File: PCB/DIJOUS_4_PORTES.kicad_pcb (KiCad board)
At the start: 2 copper layers, 180.4 x 120 mm, 59 parts, among them J1 PowerIN, J10 DOOR_LCK, J12 WIN_SW, J13 JTAG, J14 FINAL_CARRERA_UP, J15 FINAL_CARRERA_DOWN, J2 OUT_WIN, J3 ICSP, J4 CAN, J5 OUT_DOOR, J6 USART, J7 SPI, J8 RFID_COAX, SW1 DOOR_LCK, SW3 WIN_SW, U2 PIC32MK0256MCJ048-I/Y8X, U3 TCAN334D, U4 MAX22201ATC+, U5 MAX22201ATC+, Y1 ECS-3225SMV-080-GP-TR, Y2 ECS-3225SMV-080-GP-TR

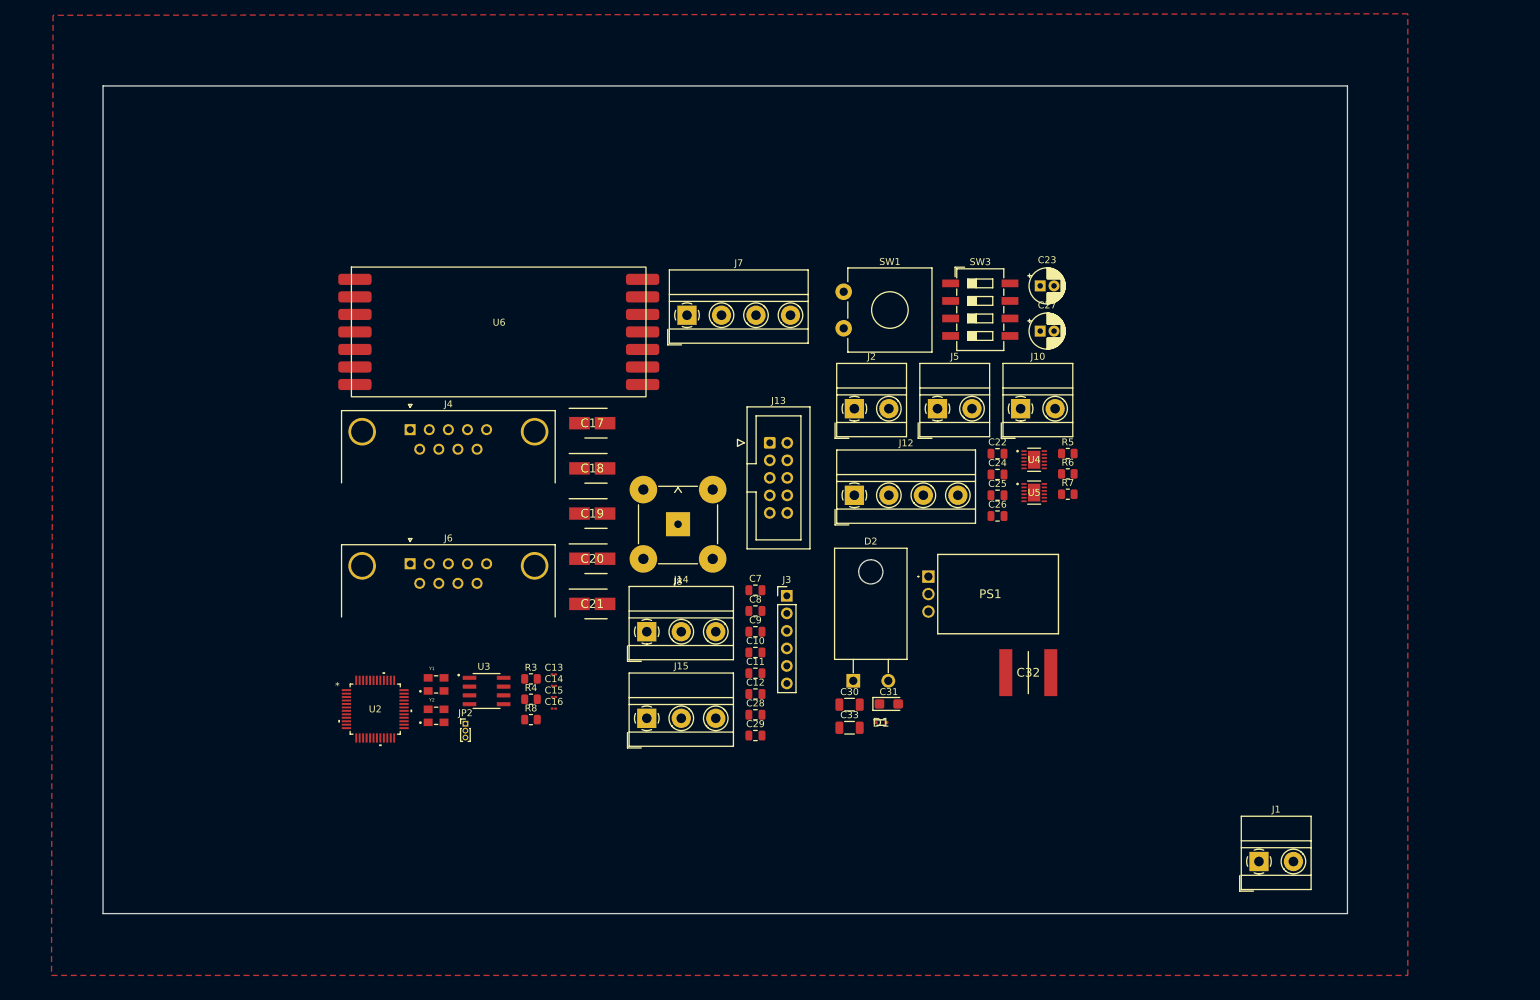
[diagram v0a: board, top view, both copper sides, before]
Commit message: power plane done
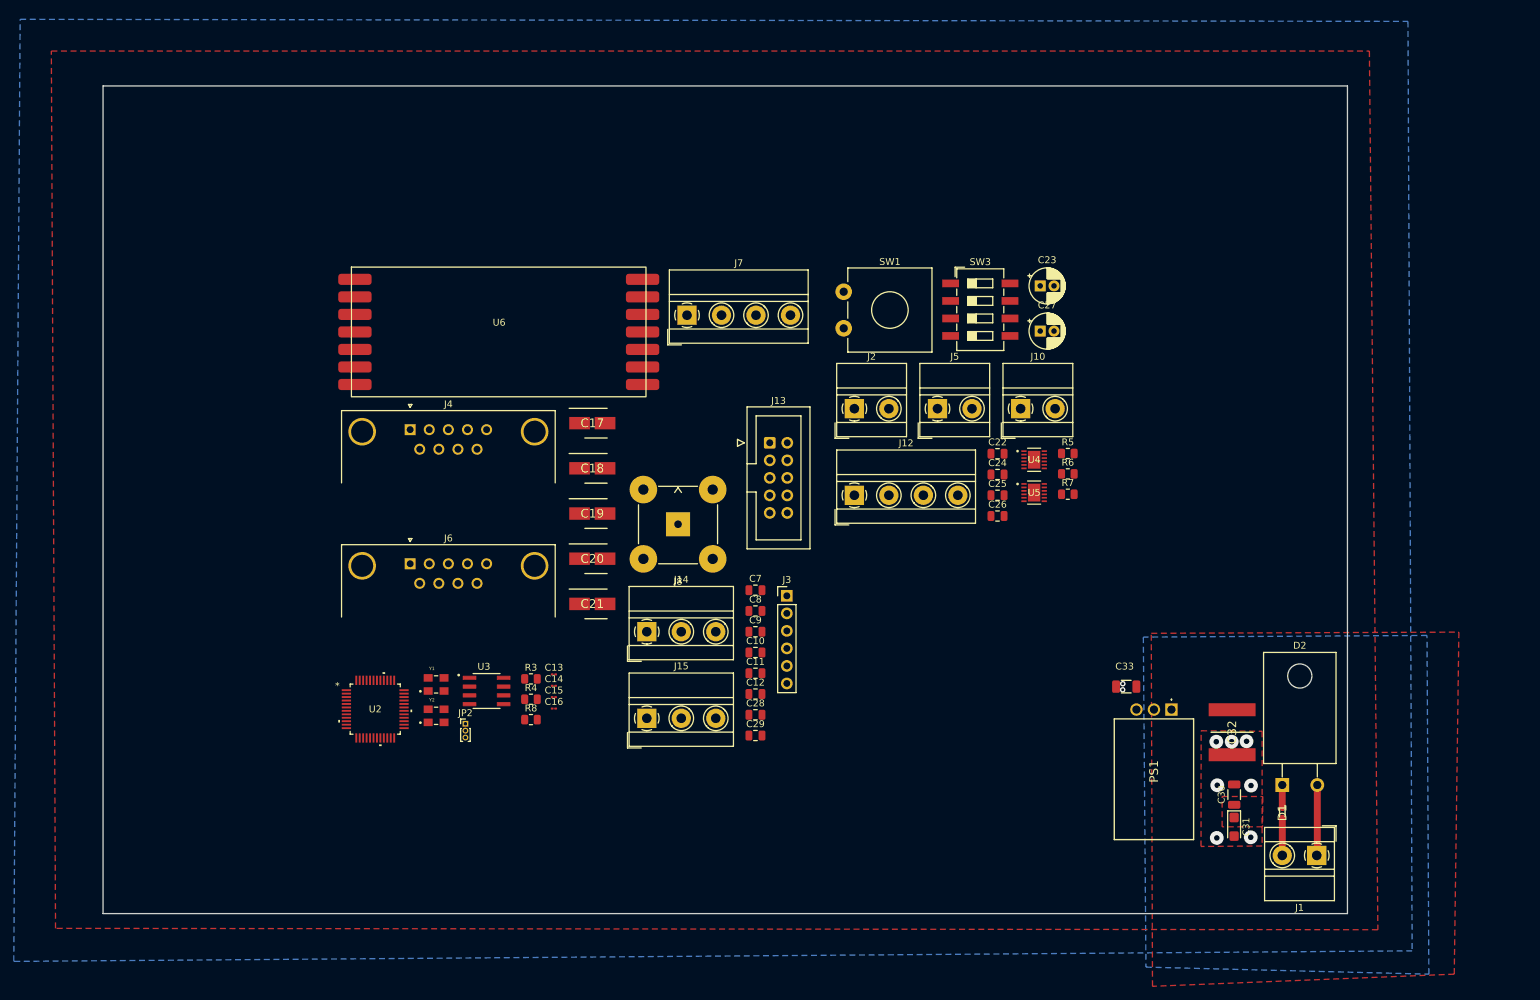
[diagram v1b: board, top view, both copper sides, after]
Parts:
- moved D2 64.0 mm to (231.1, 141.3)
- moved D1 59.6 mm to (231.1, 145.4), turned to -90 degrees
- moved C30 57.3 mm to (224.1, 142.7), turned to 90 degrees
- moved C31 53.1 mm to (224.1, 147.4), turned to -90 degrees
- moved C33 40.5 mm to (208.5, 127.1), turned to 180 degrees
- moved PS1 40.2 mm to (215.0, 130.4), turned to -90 degrees
- moved C32 30.8 mm to (223.8, 133.7), turned to -90 degrees
- moved J1 8.43 mm to (236.1, 151.6), turned to 180 degrees
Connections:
- net Net-(C12-Pad1) renamed /DIGITAL/MCLR_VDD
- net Net-(D2-A) renamed /PWR IN/pwin
- net Net-(J3-VDD) renamed /DIGITAL/Vdd_icsp
- net Net-(J8-In) renamed /DIGITAL/RF_out
- net Net-(U2-OSCI/CLKI/AN49/CVD49/RPC12/RC12') renamed /DIGITAL/clk1i
- net Net-(U2-OSCO/CLKO/RPC15/RC15) renamed /DIGITAL/clk1o
- net Net-(U2-SOSCI/RPC13/RC13) renamed /DIGITAL/clk2i
- net Net-(U2-SOSCO/RPB8/T1CK/RB8) renamed /DIGITAL/clk2o
- C18 pad 1: VDD -> VDDA
- C9 pad 2: VDD -> VDDA
- U2 pad 10: WIN_IN3 -> WIN_SW3
- U2 pad 15: VDD -> VDDA
- U2 pad 9: ISEN -> ISEN_WIN
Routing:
- net /PWR IN/pwin: track 0.00 -> 10.2 mm
- net GNDPWR: track 0.00 -> 5.84 mm, vias 0 -> 7
- net +12V: track 0.00 -> 3.26 mm
- net GND: track 0.00 -> 2.31 mm, vias 0 -> 2
- added copper zone on F.Cu, net +12V
- added copper zone on F.Cu, net +3.3V
- added copper zone on B.Cu, net GND
- added copper zone on B.Cu, net GNDPWR
- added copper zone on F.Cu, net GNDPWR
- removed copper zone on F.Cu, net GND

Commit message: start digital
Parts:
- moved J13 91.6 mm to (66.6, 75.8)
- moved J14 85.2 mm to (90.4, 49.2)
- moved J15 85.2 mm to (90.4, 61.7)
- moved J7 82.5 mm to (66.2, 48.2)
- moved J3 79.7 mm to (234.7, 88.3)
- moved Y1 56.4 mm to (164.4, 119.1), turned to 90 degrees
- moved Y2 56.1 mm to (164.5, 132.6), turned to -90 degrees
- moved U2 53.0 mm to (152.5, 126.1)
- moved J6 46.4 mm to (68.3, 138.1), turned to -90 degrees
- moved C16 42.5 mm to (166.8, 119.8)
- moved C14 40.8 mm to (165.4, 135.4), turned to -90 degrees
- moved C15 39.8 mm to (163.4, 116.5), turned to 90 degrees
- moved J4 39.5 mm to (68.3, 105.2), turned to -90 degrees
- moved C13 37.2 mm to (162.1, 132.0), turned to 180 degrees
- moved J2 36.4 mm to (197.5, 64.1)
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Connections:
- C18 pad 2: GND -> GNDA
- C9 pad 1: GND -> GNDA
- U2 pad 16: GND -> GNDA
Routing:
- net VDD: track 0.00 -> 17.4 mm
- net GND: track 2.31 -> 19.4 mm, vias 2 -> 46
- net /DIGITAL/clk1o: track 0.00 -> 14.7 mm
- net /DIGITAL/clk2o: track 0.00 -> 13.8 mm
- net +3.3V: track 0.00 -> 13.4 mm
- net /DIGITAL/clk2i: track 0.00 -> 11.9 mm
- net /DIGITAL/clk1i: track 0.00 -> 11.5 mm
- net SPI_CK: track 0.00 -> 3.83 mm, vias 0 -> 1
- net GNDA: track 0.00 -> 3.16 mm, vias 0 -> 2
- net SPI_SDI: track 0.00 -> 2.96 mm, vias 0 -> 1
- net GNDPWR: track 5.84 -> 8.43 mm
- net SPI_SDO: track 0.00 -> 2.08 mm, vias 0 -> 1
- net WIN_SW1: track 0.00 -> 1.37 mm, vias 0 -> 1
- net SPI_SS: track 0.00 -> 1.36 mm, vias 0 -> 1
- added copper zone on F.Cu, net GND
- added copper zone on B.Cu, net GNDA
- added copper zone on F.Cu, net VDD

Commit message: changed clks, pwr
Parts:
- removed C13, C14, C15, C16: 21p, Capacitor_SMD:C_01005_0402Metric
- removed J13: JTAG, Connector_IDC:IDC-Header_2x05_P2.54mm_Vertical
- added C1: 1u, Capacitor_SMD:C_0805_2012Metric, F.Cu at (202.1, 140.9)
- added C2: 100n, Capacitor_SMD:C_0805_2012Metric, F.Cu at (204.5, 140.9)
- added C3: 47u, Capacitor_THT:CP_Radial_D5.0mm_P2.00mm, F.Cu at (198.1, 154.8)
- added C4: 47u, Capacitor_THT:CP_Radial_D5.0mm_P2.00mm, F.Cu at (198.1, 148.2)
- added C5: 47u, Capacitor_THT:CP_Radial_D5.0mm_P2.00mm, F.Cu at (198.1, 141.7)
- added C6: 47u, Capacitor_THT:CP_Radial_D5.0mm_P2.00mm, F.Cu at (198.1, 135.1)
- added R_LDO1: 330, Resistor_SMD:R_0805_2012Metric_Pad1.20x1.40mm_HandSolder, F.Cu at (204.5, 136.1)
- added U1: LT1528CT-PBF, kicad_models:LT1528CT#PBF, F.Cu at (206.7, 135.1)
- PS1: value P7803-2000R-S -> P7805-2000R-S
- Y1: value ECS-3225SMV-080-GP-TR -> ASZKDV-32.768KHZ-L-T3; footprint kicad_models:OSC_ECS-3225SMV-080-GP-TR -> kicad_models:ASZKDV_ABR
- moved C22 110.4 mm to (113.2, 104.5)
- moved C23 110.4 mm to (119.4, 80.2)
- moved C24 110.4 mm to (113.2, 107.5)
- moved C25 110.4 mm to (113.2, 110.5)
- moved C26 110.4 mm to (113.2, 113.5)
- moved C27 110.4 mm to (119.4, 86.7)
- moved J12 110.4 mm to (92.4, 110.5)
- moved J2 110.4 mm to (92.4, 98.0)
- moved R5 110.4 mm to (123.4, 104.5)
- moved R6 110.4 mm to (123.4, 107.4)
- moved R7 110.4 mm to (123.4, 110.4)
- moved SW3 110.4 mm to (110.7, 83.6)
- moved J10 110.4 mm to (116.5, 98.0)
- moved J3 110.4 mm to (129.6, 122.2)
- moved J5 110.4 mm to (104.5, 98.0)
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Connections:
- C10 pad 1: VDD -> +3.3V
- C11 pad 1: VDD -> +3.3V
- C17 pad 1: VDD -> +3.3V
- C18 pad 1: VDDA -> +3.3V
- C18 pad 2: GNDA -> GND
- C19 pad 1: VDD -> +3.3V
- C20 pad 1: VDD -> +3.3V
- C21 pad 1: VDD -> +3.3V
- C33 pad 1: +3.3V -> +5V
- C33 pad 2: GND -> GNDPWR
- C7 pad 1: VDD -> +3.3V
- C8 pad 1: VDD -> +3.3V
- C9 pad 1: GNDA -> GND
- C9 pad 2: VDDA -> +3.3V
- J3 pad 2: /DIGITAL/Vdd_icsp -> +3.3V
- PS1 pad 3: +3.3V -> +5V
- R3 pad 2: VDD -> +3.3V
- U2 pad 15: VDDA -> +3.3V
- U2 pad 16: GNDA -> GND
- U2 pad 22: VDD -> +3.3V
- U2 pad 26: VDD -> +3.3V
- U2 pad 28: /DIGITAL/clk1o -> unconnected-(U2-OSCO/CLKO/RPC15/RC15-Pad28)
- U2 pad 36: /DIGITAL/clk2o -> FINAL_CARRERA_DOWN
- U2 pad 39: FINAL_CARRERA -> FINAL_CARRERA_UP
- U2 pad 43: VDD -> +3.3V
- U2 pad 6: VDD -> +3.3V
- Y1 pad 3: /DIGITAL/clk2o -> +3.3V
- Y2 pad 1: /DIGITAL/clk1i -> unconnected-(Y2-TRI-STATE-Pad1)
- Y2 pad 3: /DIGITAL/clk1o -> /DIGITAL/clk1i
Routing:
- net +3.3V: track 13.4 -> 71.5 mm
- net +5V: track 0.00 -> 23.3 mm
- net VDD: track 17.4 -> 0.00 mm
- net /DIGITAL/clk1o: track 14.7 -> 0.00 mm
- net /DIGITAL/clk2o: track 13.8 -> 0.00 mm
- net GNDA: track 3.16 -> 0.00 mm, vias 2 -> 0
- net /DIGITAL/clk1i: track 11.5 -> 9.42 mm
- net /DIGITAL/clk2i: track 11.9 -> 10.2 mm
- net GND: track 19.4 -> 20.1 mm, vias 46 -> 61
- net GNDPWR: track 8.43 -> 8.15 mm, vias 7 -> 9
- removed copper zone on B.Cu, net GNDA
- removed copper zone on F.Cu, net VDD

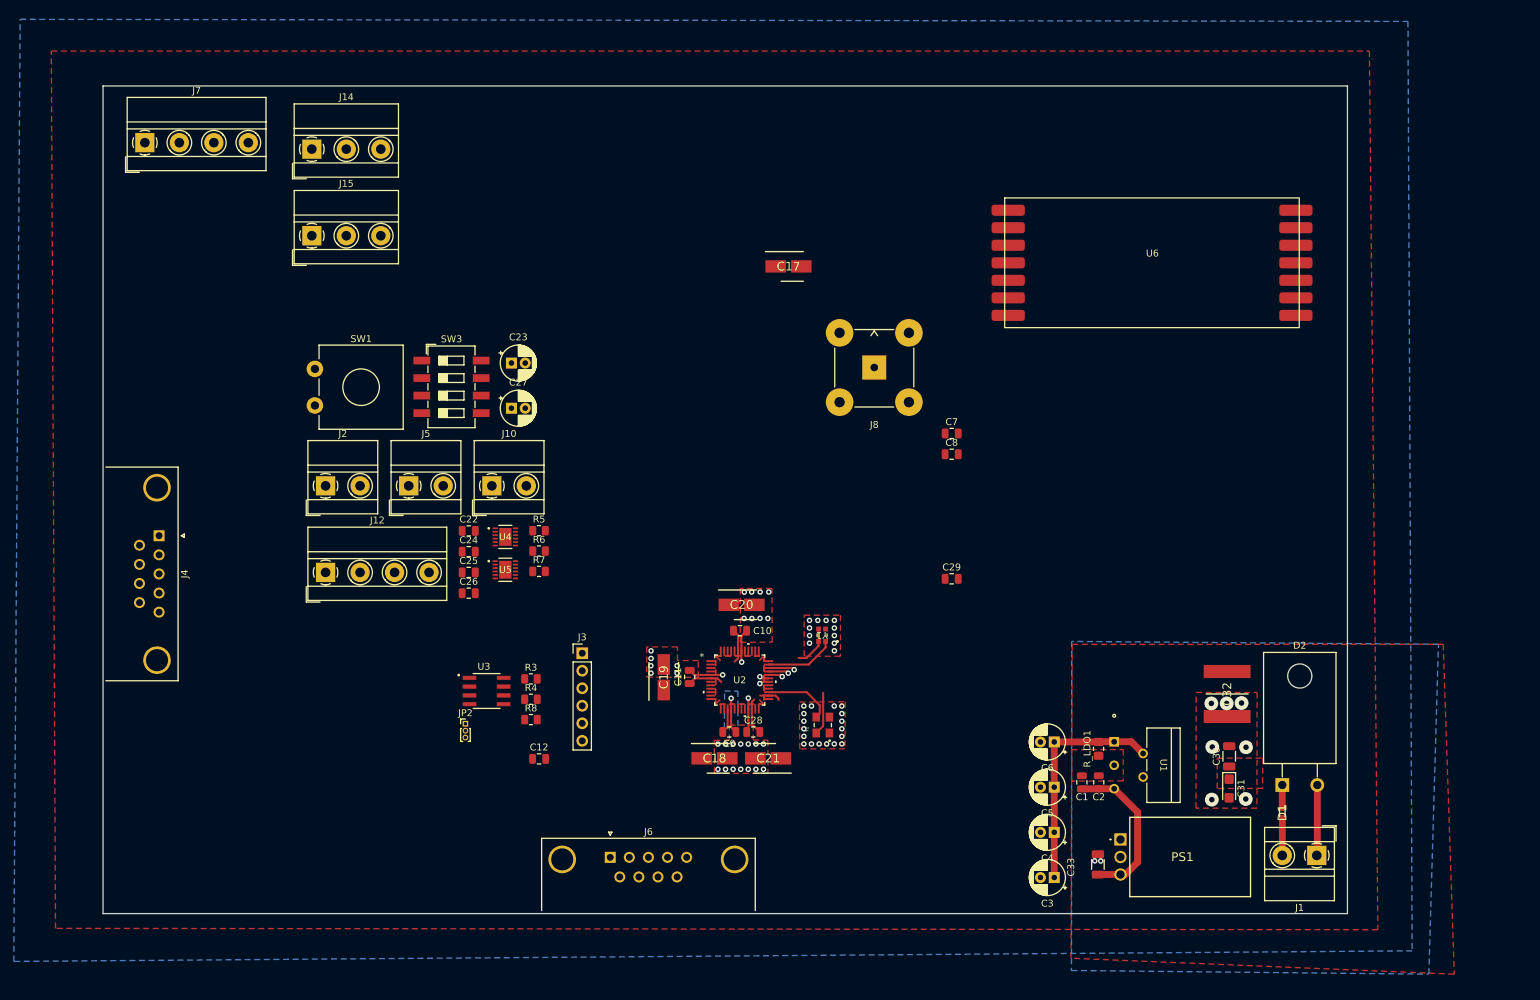
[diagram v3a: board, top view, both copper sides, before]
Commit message: canvis a sortides de potencia
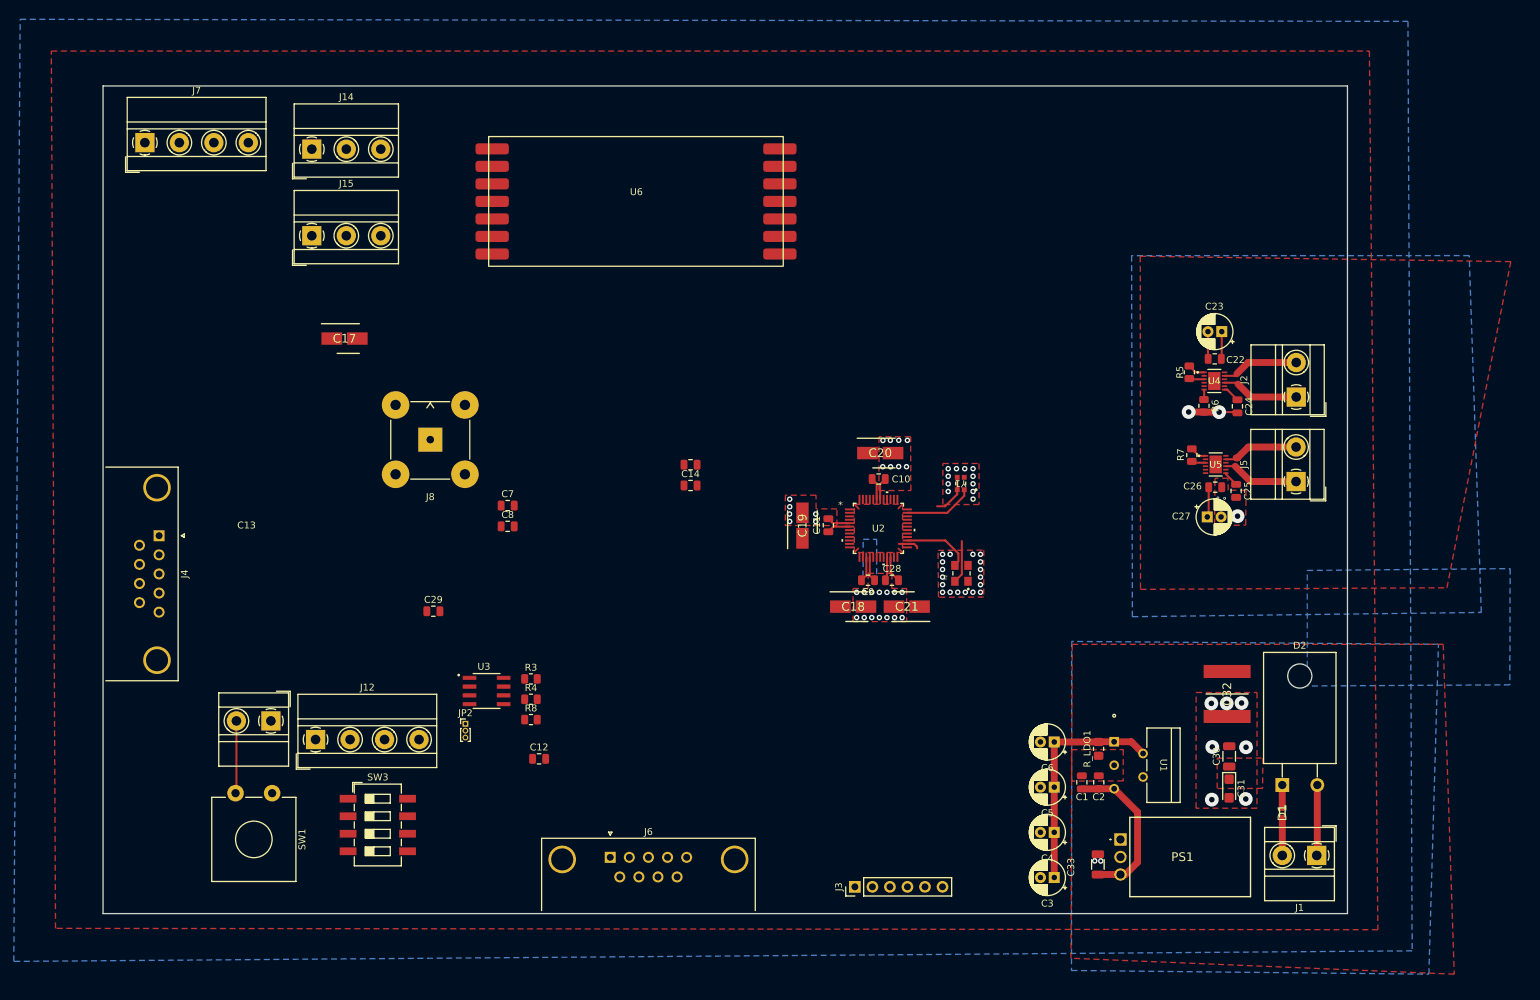
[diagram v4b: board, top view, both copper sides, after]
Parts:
- added C13: 100n, Capacitor_SMD:C_0805_2012Metric, F.Cu at (145.3, 94.9)
- added C14: 100n, Capacitor_SMD:C_0805_2012Metric, F.Cu at (145.3, 97.9)
- moved J2 141.3 mm to (233.1, 85.1), turned to 90 degrees
- moved J5 128.6 mm to (233.1, 97.3), turned to 90 degrees
- moved C24 113.4 mm to (224.6, 86.5), turned to -90 degrees
- moved C25 111.9 mm to (224.4, 98.7), turned to -90 degrees
- moved C22 111.0 mm to (221.3, 79.6), turned to 180 degrees
- moved C26 109.3 mm to (221.4, 98.2)
- moved U4 105.2 mm to (221.3, 82.8)
- moved U5 104.1 mm to (221.4, 94.9)
- moved C23 103.1 mm to (222.3, 75.6), turned to 180 degrees
- moved C27 102.1 mm to (220.2, 102.5)
- moved R6 98.7 mm to (219.8, 86.4), turned to -90 degrees
- moved R5 97.0 mm to (217.6, 81.5), turned to -90 degrees
- moved R7 96.1 mm to (218.0, 93.5), turned to -90 degrees
- moved U6 75.3 mm to (137.5, 55.9)
- moved C29 75.3 mm to (108.0, 116.2)
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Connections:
- J2 pad 1: WIN_OUT1 -> WIN_OUT2
- J2 pad 2: WIN_OUT2 -> WIN_OUT1
- J3 pad 3: GND -> Net-(J3-VSS)
- J5 pad 1: DOOR_OUT1 -> DOOR_OUT2
- J5 pad 2: DOOR_OUT2 -> DOOR_OUT1
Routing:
- net GNDPWR: track 8.15 -> 23.2 mm, vias 9 -> 16
- net DOOR_OUT1: track 0.00 -> 11.1 mm
- net DOOR_OUT2: track 0.00 -> 11.1 mm
- net WIN_OUT1: track 0.00 -> 11.1 mm
- net WIN_OUT2: track 0.00 -> 11.0 mm
- net LOCK: track 0.00 -> 10.5 mm
- net +12V: track 3.26 -> 11.8 mm
- net GND: track 20.1 -> 13.7 mm, vias 61 -> 57
- net +3.3V: track 71.5 -> 66.6 mm
- net SPI_CK: track 3.83 -> 0.00 mm, vias 1 -> 0
- net SPI_SDI: track 2.96 -> 0.00 mm, vias 1 -> 0
- net Net-(U4-ILIM): track 0.00 -> 2.54 mm
- net Net-(U4-V18): track 0.00 -> 2.49 mm
- net Net-(U5-ILIM): track 0.00 -> 2.41 mm
- net Net-(U5-V18): track 0.00 -> 2.25 mm
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
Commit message: xtra
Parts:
- removed JP2: Jumper_3_Bridged12, Connector_PinHeader_1.00mm:PinHeader_1x03_P1.00mm_Vertical
- moved U6 49.6 mm to (180.2, 81.1), turned to 180 degrees
- moved C10 14.0 mm to (186.4, 99.4)
- moved C11 14.0 mm to (179.1, 106.1)
- moved C18 14.0 mm to (182.7, 117.9)
- moved C19 14.0 mm to (175.3, 106.1)
- moved C20 14.0 mm to (186.6, 95.6)
- moved C21 14.0 mm to (190.4, 117.9)
- moved C28 14.0 mm to (188.3, 114.0)
- moved C9 14.0 mm to (184.8, 114.0)
- moved U2 14.0 mm to (186.3, 106.5)
- moved Y1 14.0 mm to (198.2, 100.0)
- moved Y2 14.0 mm to (198.4, 113.0)
- moved C22 4.31 mm to (221.3, 83.9)
- moved C23 4.31 mm to (222.3, 79.9)
- moved C24 4.31 mm to (224.6, 90.8)
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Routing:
- net DOOR_IN1: track 0.00 -> 35.8 mm, vias 0 -> 2
- net DOOR_IN2: track 0.00 -> 35.6 mm, vias 0 -> 2
